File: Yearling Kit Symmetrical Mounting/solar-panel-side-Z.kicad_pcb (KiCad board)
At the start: 4 copper layers, 100 x 100 mm, 45 parts, among them J1 CON-5040500591, J2 Screw_Terminal_01x02, J3 Screw_Terminal_01x02, J4 Conn_01x01, J5 Conn_01x01, J6 Conn_01x01, J7 Conn_01x01, U1 VEML7700, U2 DRV2605LDGS, U3 MCP9808_DFN, U4 AD8495, U5 ADS1015IDGS, U6 TLVH431 DBZ SOT-23

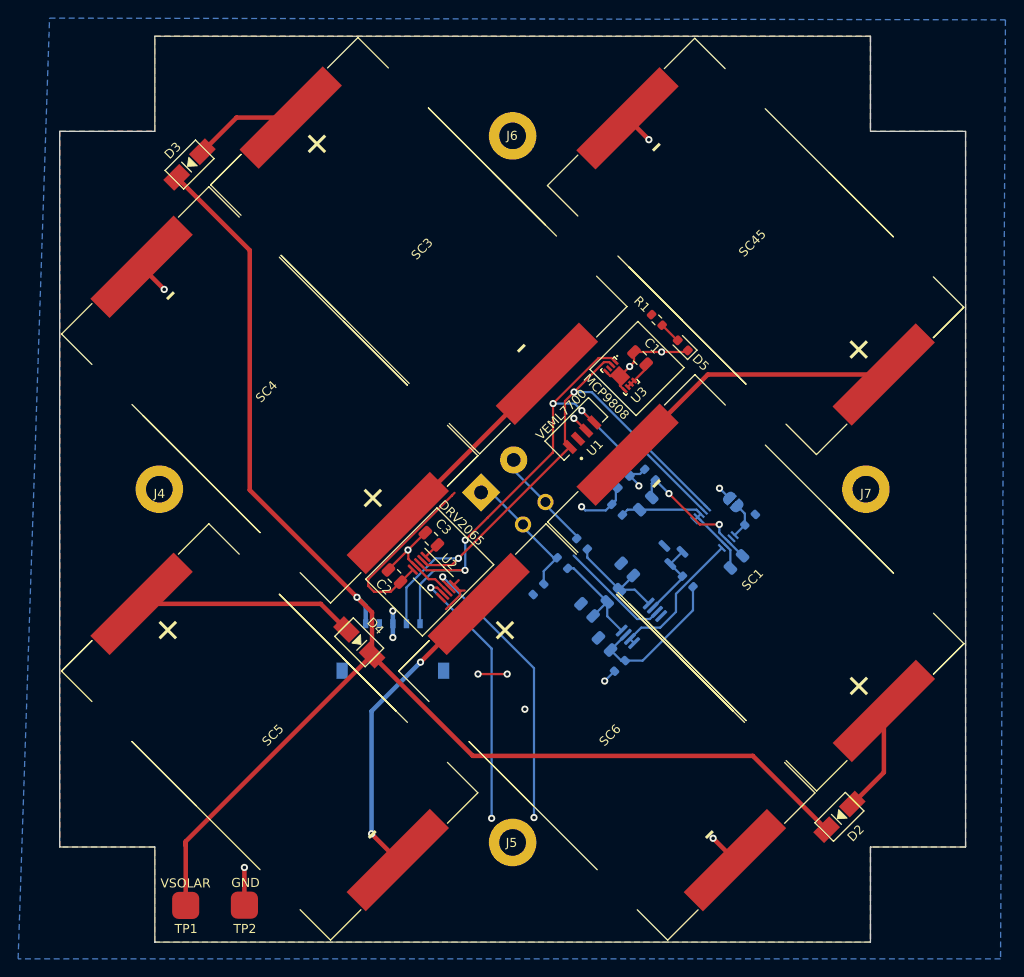
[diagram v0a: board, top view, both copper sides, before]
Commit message: -Z Face Mounting Changed
Holes are now symmetrical.
Typos in Silkscreen have been corrected.
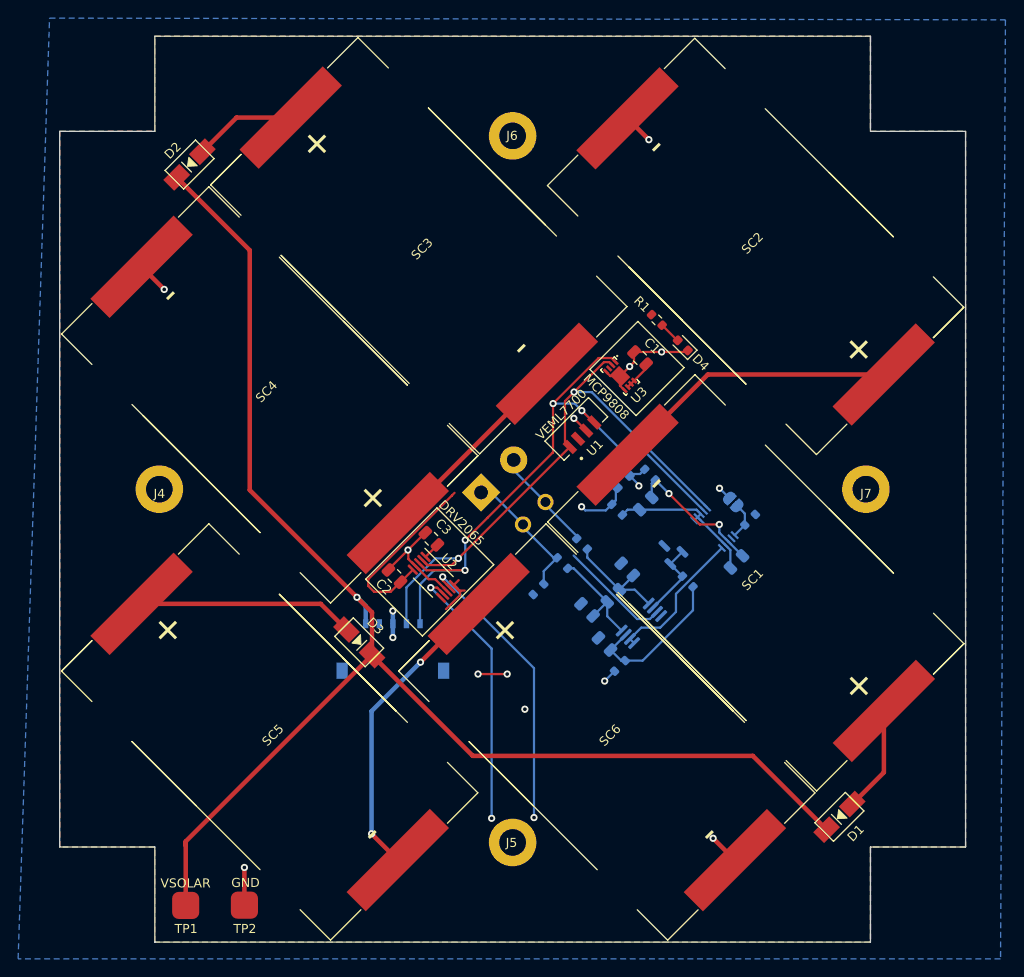
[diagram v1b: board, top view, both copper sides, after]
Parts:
- renumbered D2 to D1, D3 to D2, D4 to D3, D5 to D4, SC45 to SC2
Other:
- board text added: "R2 = 1M-Ohm R3 = 100-Ohm R4 = 100-Ohm R5 = 1k-Ohm R6 = 10k-Ohm"
- board text removed: "R2 = 10M-Ohm R3 = 100-Ohm R4 = 100-Ohm R5 = 1k-Ohm R6 = 10k-Ohm"
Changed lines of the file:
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@@
   (net 19 "Net-(U2-Pad7)")
   (net 20 "unconnected-(U3-Pad3)")
-  (net 21 "Net-(D5-Pad2)")
+  (net 21 "Net-(D1-Pad2)")
   (net 22 "Net-(C4-Pad1)")
   (net 23 "Net-(J2-Pad1)")
@@
     (property "Sheetname" "")
     (attr smd)
-    (fp_text reference "D3" (at -0.220315 -2.404163 45) (layer "F.SilkS")
+    (fp_text reference "D2" (at -0.220315 -2.404163 45) (layer "F.SilkS")
       (effects (font (size 1 1) (thickness 0.15)))
     )
@@
       (net 3 "VSOLAR") (pinfunction "K") (pintype "passive"))
     (pad "2" smd rect locked (at 2 0 45) (size 2.5 1.7) (layers "F.Cu" "F.Paste" "F.Mask")
-      (net 7 "Net-(D3-Pad2)") (pinfunction "A") (pintype "passive"))
+      (net 6 "Net-(D2-Pad2)") (pinfunction "A") (pintype "passive"))
     (model "${KIPRJMOD}/Extras/3-DComponents/CDBA240LL-HF.STEP"
       (offset (xyz -2.5 1.25 0))
@@
     (property "Sheetname" "")
     (attr smd)
-    (fp_text reference "D5" (at -2.735 0.06 135) (layer "F.SilkS")
+    (fp_text reference "D4" (at -2.735 0.06 135) (layer "F.SilkS")
       (effects (font (size 1 1) (thickness 0.15)))
     )
@@
       (net 1 "GND") (pinfunction "K") (pintype "passive"))
     (pad "2" smd roundrect (at 0.7875 0 135) (size 0.875 0.95) (layers "F.Cu" "F.Paste" "F.Mask") (roundrect_rratio 0.25)
-      (net 21 "Net-(D5-Pad2)") (pinfunction "A") (pintype "passive"))
+      (net 8 "Net-(D4-Pad2)") (pinfunction "A") (pintype "passive"))
     (model "${KICAD6_3DMODEL_DIR}/LED_SMD.3dshapes/LED_0603_1608Metric.wrl"
       (offset (xyz 0 0 0))
@@
     (fp_line (start 0 0) (end 11.5 0) (layer "Dwgs.User") (width 0.12))
     (pad "1" smd rect (at 0 -20 45) (size 13 3) (layers "F.Cu" "F.Paste" "F.Mask")
-      (net 8 "Net-(D4-Pad2)") (pinfunction "+") (pintype "passive"))
+      (net 7 "Net-(D3-Pad2)") (pinfunction "+") (pintype "passive"))
     (pad "2" smd rect (at 0 20 45) (size 13 3) (layers "F.Cu" "F.Paste" "F.Mask")
       (net 17 "Net-(SC5-Pad2)") (pinfunction "-") (pintype "passive"))
@@
     (fp_line (start 11.5 21) (end 11.5 0) (layer "Dwgs.User") (width 0.12))
     (pad "1" smd rect (at 0 -20 45) (size 13 3) (layers "F.Cu" "F.Paste" "F.Mask")
-      (net 7 "Net-(D3-Pad2)") (pinfunction "+") (pintype "passive"))
+      (net 6 "Net-(D2-Pad2)") (pinfunction "+") (pintype "passive"))
     (pad "2" smd rect (at 0 20 45) (size 13 3) (layers "F.Cu" "F.Paste" "F.Mask")
       (net 16 "Net-(SC3-Pad2)") (pinfunction "-") (pintype "passive"))
@@
       (net 2 "+3V3") (pintype "passive"))
     (pad "2" smd roundrect (at 0.825 0 315) (size 0.8 0.95) (layers "F.Cu" "F.Paste" "F.Mask") (roundrect_rratio 0.25)
-      (net 21 "Net-(D5-Pad2)") (pintype "passive"))
+      (net 8 "Net-(D4-Pad2)") (pintype "passive"))
     (model "${KICAD6_3DMODEL_DIR}/Resistor_SMD.3dshapes/R_0603_1608Metric.wrl"
       (offset (xyz 0 0 0))
@@
     (property "Sheetname" "")
     (attr smd)
-    (fp_text reference "D4" (at 0 2.54 135) (layer "F.SilkS")
+    (fp_text reference "D3" (at 0 2.54 135) (layer "F.SilkS")
       (effects (font (size 1 1) (thickness 0.15)))
     )
@@
       (net 3 "VSOLAR") (pinfunction "K") (pintype "passive"))
     (pad "2" smd rect locked (at 2 0 135) (size 2.5 1.7) (layers "F.Cu" "F.Paste" "F.Mask")
-      (net 8 "Net-(D4-Pad2)") (pinfunction "A") (pintype "passive"))
+      (net 7 "Net-(D3-Pad2)") (pinfunction "A") (pintype "passive"))
     (model "${KIPRJMOD}/Extras/3-DComponents/CDBA240LL-HF.STEP"
       (offset (xyz -2.5 1.25 0))
@@
     (property "Sheetname" "")
     (attr through_hole)
-    (fp_text reference "SC45" (at 0 0.5 45) (layer "F.SilkS")
+    (fp_text reference "SC2" (at 0 0.5 45) (layer "F.SilkS")
       (effects (font (size 1 1) (thickness 0.15)))
     )
@@
     (property "Sheetname" "")
     (attr smd)
-    (fp_text reference "D2" (at 0 2.54 45) (layer "F.SilkS")
+    (fp_text reference "D1" (at 0 2.54 45) (layer "F.SilkS")
       (effects (font (size 1 1) (thickness 0.15)))
     )
@@
       (net 3 "VSOLAR") (pinfunction "K") (pintype "passive"))
     (pad "2" smd rect locked (at 2 0 45) (size 2.5 1.7) (layers "F.Cu" "F.Paste" "F.Mask")
-      (net 6 "Net-(D2-Pad2)") (pinfunction "A") (pintype "passive"))
+      (net 21 "Net-(D1-Pad2)") (pinfunction "A") (pintype "passive"))
     (model "${KIPRJMOD}/Extras/3-DComponents/CDBA240LL-HF.STEP"
       (offset (xyz -2.5 1.25 0))
@@
     (fp_line (start 0 -21) (end 0 -20) (layer "Dwgs.User") (width 0.12))
     (pad "1" smd rect (at 0 -20 225) (size 13 3) (layers "F.Cu" "F.Paste" "F.Mask")
-      (net 6 "Net-(D2-Pad2)") (pinfunction "+") (pintype "passive"))
+      (net 21 "Net-(D1-Pad2)") (pinfunction "+") (pintype "passive"))
     (pad "2" smd rect (at 0 20 225) (size 13 3) (layers "F.Cu" "F.Paste" "F.Mask")
       (net 15 "Net-(SC1-Pad2)") (pinfunction "-") (pintype "passive"))
@@
     (effects (font (size 1 1) (thickness 0.15)) (justify mirror))
   )
-  (gr_text "R2 = 10M-Ohm\nR3 = 100-Ohm\nR4 = 100-Ohm\nR5 = 1k-Ohm\nR6 = 10k-Ohm" (at 114.57 109.090001) (layer "B.SilkS")
+  (gr_text "R2 = 1M-Ohm\nR3 = 100-Ohm\nR4 = 100-Ohm\nR5 = 1k-Ohm\nR6 = 10k-Ohm" (at 114.57 109.090001) (layer "B.SilkS")
     (effects (font (size 1 1) (thickness 0.15)) (justify left mirror))
   )
@@
   (segment (start 140.978604 92.641396) (end 137.778501 95.841499) (width 0.25) (layer "B.Cu") (net 5))
   (segment (start 158.222469 74.28) (end 170.972561 87.030093) (width 0.25) (layer "B.Cu") (net 5))
-  (segment (start 190.48 109.48) (end 190.48 116.27) (width 0.5) (layer "F.Cu") (net 6))
-  (segment (start 190.48 116.27) (end 186.99 119.76) (width 0.5) (layer "F.Cu") (net 6))
-  (segment (start 125 43.98) (end 119.02 43.98) (width 0.5) (layer "F.Cu") (net 7))
-  (segment (start 119.02 43.98) (end 115.25 47.75) (width 0.5) (layer "F.Cu") (net 7))
-  (segment (start 108.537864 97.657864) (end 128.317864 97.657864) (width 0.5) (layer "F.Cu") (net 8))
-  (segment (start 128.317864 97.657864) (end 131.15 100.49) (width 0.5) (layer "F.Cu") (net 8))
+  (segment (start 125 43.98) (end 119.02 43.98) (width 0.5) (layer "F.Cu") (net 6))
+  (segment (start 119.02 43.98) (end 115.25 47.75) (width 0.5) (layer "F.Cu") (net 6))
+  (segment (start 108.537864 97.657864) (end 128.317864 97.657864) (width 0.5) (layer "F.Cu") (net 7))
+  (segment (start 128.317864 97.657864) (end 131.15 100.49) (width 0.5) (layer "F.Cu") (net 7))
+  (segment (start 166.002732 66.899302) (end 167.669736 68.566306) (width 0.25) (layer "F.Cu") (net 8))
   (segment (start 159.941698 99.022624) (end 161.532688 100.613613) (width 0.25) (layer "B.Cu") (net 11))
   (segment (start 158.386061 98.994339) (end 159.941698 97.438705) (width 0.25) (layer "B.Cu") (net 11))
@@
   (segment (start 151.86 104.76) (end 151.86 121.25) (width 0.25) (layer "B.Cu") (net 19))
   (segment (start 141.78 94.68) (end 151.86 104.76) (width 0.25) (layer "B.Cu") (net 19))
-  (segment (start 166.002732 66.899302) (end 167.669736 68.566306) (width 0.25) (layer "F.Cu") (net 21))
+  (segment (start 190.48 109.48) (end 190.48 116.27) (width 0.5) (layer "F.Cu") (net 21))
+  (segment (start 190.48 116.27) (end 186.99 119.76) (width 0.5) (layer "F.Cu") (net 21))
   (segment (start 161.992307 101.073233) (end 160.309392 102.756148) (width 0.25) (layer "B.Cu") (net 22))
   (segment (start 169.409857 98.365014) (end 169.409856 95.777004) (width 0.25) (layer "B.Cu") (net 22))
